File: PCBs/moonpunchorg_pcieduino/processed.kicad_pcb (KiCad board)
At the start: 2 copper layers, 51 x 30 mm, 32 parts, among them J1 PCIE-MINI, J2 ISP, J3 DIGITAL, J4 ANALOG_POWER, SW1 Reset, U1 ATMEGA32U4, X1 8MHz

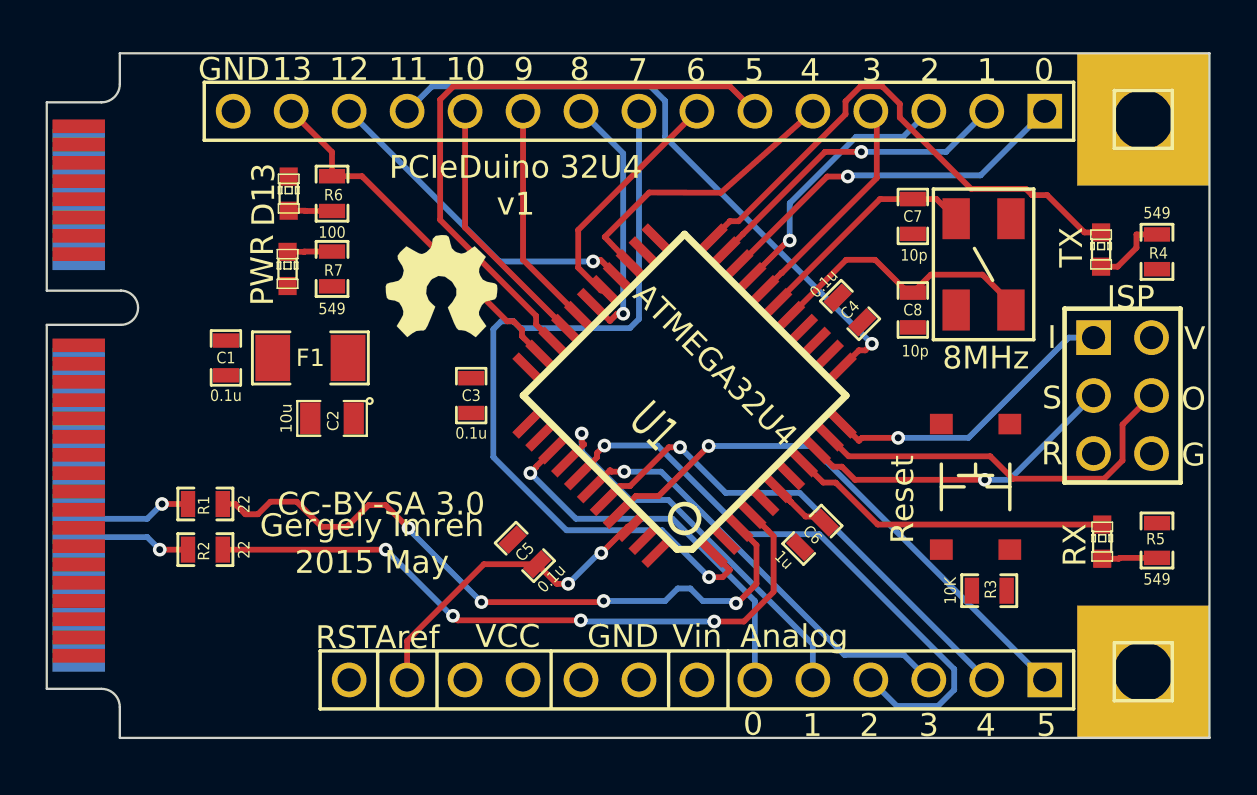
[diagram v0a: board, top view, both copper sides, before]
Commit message: recheck all circuits and clean up fill zone by rerouting the nets using freerouting and manually
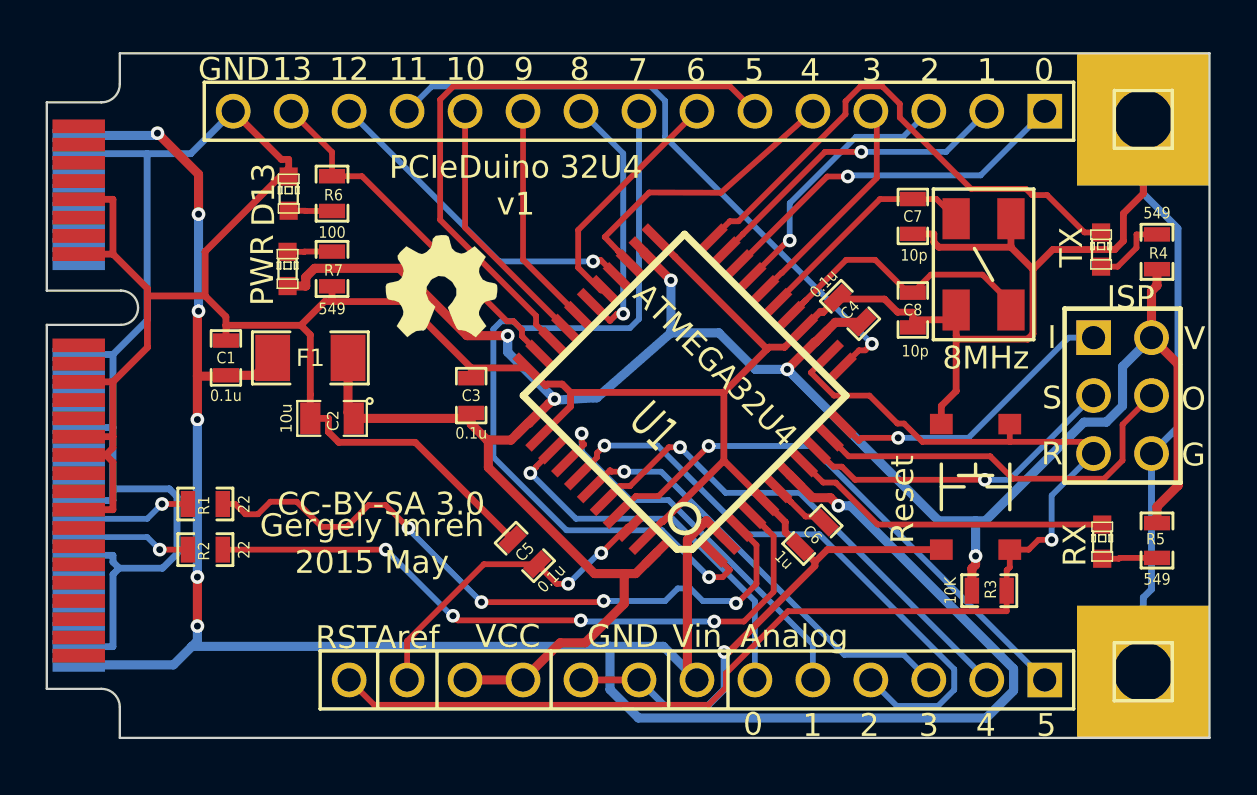
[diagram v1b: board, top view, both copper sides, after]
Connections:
- C1 pad 1: (no net) -> /UVCC
- C1 pad 2: (no net) -> GND
- C2 pad 1: (no net) -> VCC
- C2 pad 2: (no net) -> GND
- C3 pad 1: (no net) -> VCC
- C3 pad 2: (no net) -> GND
- C4 pad 1: (no net) -> VCC
- C4 pad 2: (no net) -> GND
- C5 pad 2: (no net) -> GND
- C6 pad 2: (no net) -> GND
- C7 pad 2: (no net) -> GND
- C8 pad 2: (no net) -> GND
- D3 pad 2: (no net) -> GND
- D4 pad 1: (no net) -> VCC
- F1 pad 1: (no net) -> /UVCC
- F1 pad 2: (no net) -> VCC
- J1 pad 15: (no net) -> GND
- J1 pad 18: (no net) -> GND
- J1 pad 2: (no net) -> /UVCC
- J1 pad 21: (no net) -> GND
- J1 pad 26: (no net) -> GND
- J1 pad 27: (no net) -> GND
- J1 pad 29: (no net) -> GND
- J1 pad 34: (no net) -> GND
- J1 pad 35: (no net) -> GND
- J1 pad 4: (no net) -> GND
- J1 pad 40: (no net) -> GND
- J1 pad 50: (no net) -> GND
- J1 pad 52: (no net) -> /UVCC
- J1 pad 9: (no net) -> GND
- J2 pad 2: (no net) -> VCC
- J2 pad 5: (no net) -> /RESET
- J2 pad 6: (no net) -> GND
- J3 pad 15: (no net) -> GND
- J4 pad 10: (no net) -> VCC
- J4 pad 11: (no net) -> VCC
- J4 pad 13: (no net) -> /RESET
- J4 pad 7: (no net) -> /UVCC
- J4 pad 8: (no net) -> GND
- J4 pad 9: (no net) -> GND
- MOUNTING_HOLE1 pad 1: (no net) -> GND
- MOUNTING_HOLE2 pad 1: (no net) -> GND
- R3 pad 1: (no net) -> VCC
- R3 pad 2: (no net) -> /RESET
- R4 pad 2: (no net) -> VCC
- R5 pad 2: (no net) -> VCC
- R7 pad 2: (no net) -> GND
- SW1 pad 1: (no net) -> GND
- SW1 pad 2: (no net) -> /RESET
- U1 pad 13: (no net) -> /RESET
- U1 pad 14: (no net) -> VCC
- U1 pad 15: (no net) -> GND
- U1 pad 2: (no net) -> /UVCC
- U1 pad 23: (no net) -> GND
- U1 pad 24: (no net) -> VCC
- U1 pad 33: (no net) -> GND
- U1 pad 34: (no net) -> VCC
- U1 pad 35: (no net) -> GND
- U1 pad 43: (no net) -> GND
- U1 pad 44: (no net) -> VCC
- U1 pad 5: (no net) -> GND
- U1 pad 7: (no net) -> /UVCC
- X1 pad 3: (no net) -> GND
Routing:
- net GND: track 0.00 -> 235.1 mm, vias 0 -> 1
- net VCC: track 0.00 -> 107.2 mm, vias 0 -> 5
- net /UVCC: track 0.00 -> 102.0 mm, vias 0 -> 7
- net /RESET: track 0.00 -> 56.9 mm, vias 0 -> 1
- net N-0000018: track 12.5 -> 13.4 mm
- net /D4: track 13.0 -> 13.8 mm
- net /MOSI: track 17.4 -> 18.0 mm
- net /TXLED: track 23.1 -> 23.7 mm
- net /MISO: track 13.2 -> 13.8 mm
- net /D11: track 28.2 -> 28.7 mm
- net /D1/TXO: track 14.0 -> 14.6 mm
- net /D7: track 35.3 -> 35.8 mm
- net /SCK: track 14.3 -> 14.8 mm
